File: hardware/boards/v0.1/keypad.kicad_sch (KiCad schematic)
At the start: 78 parts, among them SW1 TRIG1, SW10 TRIG10, SW11 TRIG11, SW12 TRIG12, SW13 TRIG13, SW14 TRIG14, SW15 TRIG15, SW16 TRIG16, SW17 MENU0, SW19 MENU1, SW2 TRIG2, SW20 MENU2, SW21 MENU3, SW3 TRIG3, SW4 TRIG4, SW5 TRIG5, SW6 TRIG6, SW7 TRIG7, SW8 TRIG8, SW9 TRIG9, U25 TCA8418RTWR, U38 ADS7128IRTER

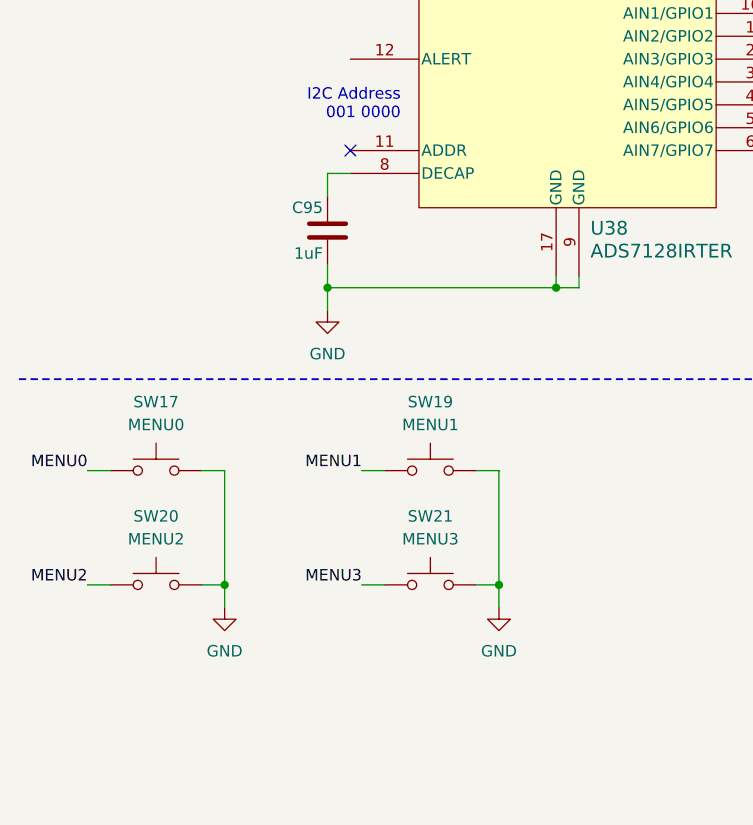
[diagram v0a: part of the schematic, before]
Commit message: feat: more routing and DRC cleanup
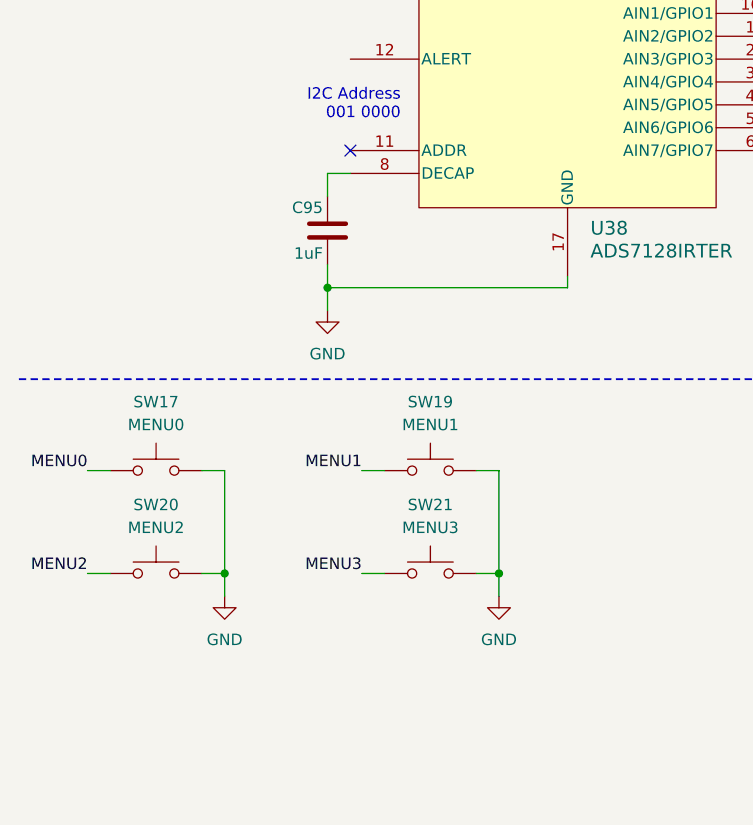
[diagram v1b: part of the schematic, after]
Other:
- moved on the sheet: SW20, SW21
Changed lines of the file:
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@@
 	)
 	(junction
-		(at 72.39 156.21)
-		(diameter 0)
-		(color 0 0 0 0)
-	)
-	(junction
-		(at 35.56 189.23)
+		(at 35.56 187.96)
 		(diameter 0)
 		(color 0 0 0 0)
@@
 	)
 	(junction
-		(at 66.04 189.23)
+		(at 66.04 187.96)
 		(diameter 0)
 		(color 0 0 0 0)
@@
 	(wire
 		(pts
-			(xy 46.99 156.21) (xy 72.39 156.21)
-		)
-		(stroke
-			(width 0)
-			(type default)
-		)
-	)
-	(wire
-		(pts
 			(xy 20.32 176.53) (xy 22.86 176.53)
 		)
@@
 	(wire
 		(pts
-			(xy 66.04 176.53) (xy 66.04 189.23)
+			(xy 66.04 176.53) (xy 66.04 187.96)
 		)
 		(stroke
@@
 	(wire
 		(pts
-			(xy 20.32 189.23) (xy 22.86 189.23)
+			(xy 20.32 187.96) (xy 22.86 187.96)
 		)
 		(stroke
@@
 	(wire
 		(pts
-			(xy 63.5 189.23) (xy 66.04 189.23)
+			(xy 63.5 187.96) (xy 66.04 187.96)
 		)
 		(stroke
@@
 	(wire
 		(pts
-			(xy 72.39 154.94) (xy 72.39 156.21)
-		)
-		(stroke
-			(width 0)
-			(type default)
-		)
-	)
-	(wire
-		(pts
 			(xy 198.12 81.28) (xy 200.66 81.28)
 		)
@@
 	(wire
 		(pts
-			(xy 35.56 176.53) (xy 35.56 189.23)
+			(xy 35.56 176.53) (xy 35.56 187.96)
 		)
 		(stroke
@@
 	(wire
 		(pts
-			(xy 33.02 189.23) (xy 35.56 189.23)
+			(xy 33.02 187.96) (xy 35.56 187.96)
 		)
 		(stroke
@@
 	(wire
 		(pts
-			(xy 50.8 189.23) (xy 53.34 189.23)
+			(xy 50.8 187.96) (xy 53.34 187.96)
 		)
 		(stroke
@@
 	(wire
 		(pts
-			(xy 72.39 156.21) (xy 74.93 156.21)
+			(xy 46.99 156.21) (xy 73.66 156.21)
 		)
 		(stroke
@@
 	(wire
 		(pts
-			(xy 35.56 189.23) (xy 35.56 191.77)
+			(xy 35.56 187.96) (xy 35.56 190.5)
 		)
 		(stroke
@@
 	(wire
 		(pts
-			(xy 66.04 189.23) (xy 66.04 191.77)
+			(xy 66.04 187.96) (xy 66.04 190.5)
 		)
 		(stroke
@@
 	(wire
 		(pts
-			(xy 74.93 154.94) (xy 74.93 156.21)
+			(xy 162.56 142.24) (xy 163.83 142.24)
 		)
 		(stroke
@@
 	(wire
 		(pts
-			(xy 162.56 142.24) (xy 163.83 142.24)
+			(xy 137.16 35.56) (xy 135.89 35.56)
 		)
 		(stroke
@@
 	(wire
 		(pts
-			(xy 137.16 35.56) (xy 135.89 35.56)
+			(xy 162.56 66.04) (xy 161.29 66.04)
 		)
 		(stroke
@@
 	(wire
 		(pts
-			(xy 162.56 66.04) (xy 161.29 66.04)
+			(xy 134.62 134.62) (xy 138.43 134.62)
 		)
 		(stroke
@@
 	(wire
 		(pts
-			(xy 134.62 134.62) (xy 138.43 134.62)
+			(xy 73.66 154.94) (xy 73.66 156.21)
 		)
 		(stroke
@@
 	)
 	(label "MENU2"
-		(at 20.32 189.23 180)
+		(at 20.32 187.96 180)
 		(effects
 			(font
@@
 	)
 	(label "MENU3"
-		(at 50.8 189.23 180)
+		(at 50.8 187.96 180)
 		(effects
 			(font
@@
 	(symbol
 		(lib_id "Switch:SW_Push")
-		(at 58.42 189.23 0)
+		(at 58.42 187.96 0)
 		(unit 1)
 		(exclude_from_sim no)
@@
 		(fields_autoplaced yes)
 		(property "Reference" "SW21"
-			(at 58.42 181.61 0)
+			(at 58.42 180.34 0)
 			(effects
 				(font
@@
 		)
 		(property "Value" "MENU3"
-			(at 58.42 184.15 0)
+			(at 58.42 182.88 0)
 			(effects
 				(font
@@
 		)
 		(property "Footprint" "Button_Switch_SMD:SW_SPST_B3S-1000"
-			(at 58.42 184.15 0)
+			(at 58.42 182.88 0)
 			(effects
 				(font
@@
 		)
 		(property "Datasheet" "~"
-			(at 58.42 184.15 0)
+			(at 58.42 182.88 0)
 			(effects
 				(font
@@
 		)
 		(property "Description" "Push button switch, generic, two pins"
-			(at 58.42 189.23 0)
+			(at 58.42 187.96 0)
 			(effects
 				(font
@@
 		)
 		(property "MANUFACTURER" ""
-			(at 58.42 189.23 0)
+			(at 58.42 187.96 0)
 			(effects
 				(font
@@
 		)
 		(property "MAXIMUM_PACKAGE_HEIGHT" ""
-			(at 58.42 189.23 0)
+			(at 58.42 187.96 0)
 			(effects
 				(font
@@
 		)
 		(property "PARTREV" ""
-			(at 58.42 189.23 0)
+			(at 58.42 187.96 0)
 			(effects
 				(font
@@
 		)
 		(property "STANDARD" ""
-			(at 58.42 189.23 0)
+			(at 58.42 187.96 0)
 			(effects
 				(font
@@
 		)
 		(property "Connector" ""
-			(at 58.42 189.23 0)
+			(at 58.42 187.96 0)
 			(effects
 				(font
@@
 	(symbol
 		(lib_id "power:GND")
-		(at 66.04 191.77 0)
+		(at 66.04 190.5 0)
 		(unit 1)
 		(exclude_from_sim no)
@@
 		(dnp no)
 		(property "Reference" "#PWR042"
-			(at 66.04 198.12 0)
+			(at 66.04 196.85 0)
 			(effects
 				(font
@@
 		)
 		(property "Value" "GND"
-			(at 66.04 196.596 0)
+			(at 66.04 195.326 0)
 			(effects
 				(font
@@
 		)
 		(property "Footprint" ""
-			(at 66.04 191.77 0)
+			(at 66.04 190.5 0)
 			(effects
 				(font
@@
 		)
 		(property "Datasheet" ""
-			(at 66.04 191.77 0)
+			(at 66.04 190.5 0)
 			(effects
 				(font
@@
 		)
 		(property "Description" "Power symbol creates a global label with name \"GND\" , ground"
-			(at 66.04 191.77 0)
+			(at 66.04 190.5 0)
 			(effects
 				(font
@@
 	(symbol
 		(lib_id "Switch:SW_Push")
-		(at 27.94 189.23 0)
+		(at 27.94 187.96 0)
 		(unit 1)
 		(exclude_from_sim no)
@@
 		(fields_autoplaced yes)
 		(property "Reference" "SW20"
-			(at 27.94 181.61 0)
+			(at 27.94 180.34 0)
 			(effects
 				(font
@@
 		)
 		(property "Value" "MENU2"
-			(at 27.94 184.15 0)
+			(at 27.94 182.88 0)
 			(effects
 				(font
@@
 		)
 		(property "Footprint" "Button_Switch_SMD:SW_SPST_B3S-1000"
-			(at 27.94 184.15 0)
+			(at 27.94 182.88 0)
 			(effects
 				(font
@@
 		)
 		(property "Datasheet" "~"
-			(at 27.94 184.15 0)
+			(at 27.94 182.88 0)
 			(effects
 				(font
@@
 		)
 		(property "Description" "Push button switch, generic, two pins"
-			(at 27.94 189.23 0)
+			(at 27.94 187.96 0)
 			(effects
 				(font
@@
 		)
 		(property "MANUFACTURER" ""
-			(at 27.94 189.23 0)
+			(at 27.94 187.96 0)
 			(effects
 				(font
@@
 		)
 		(property "MAXIMUM_PACKAGE_HEIGHT" ""
-			(at 27.94 189.23 0)
+			(at 27.94 187.96 0)
 			(effects
 				(font
@@
 		)
 		(property "PARTREV" ""
-			(at 27.94 189.23 0)
+			(at 27.94 187.96 0)
 			(effects
 				(font
@@
 		)
 		(property "STANDARD" ""
-			(at 27.94 189.23 0)
+			(at 27.94 187.96 0)
 			(effects
 				(font
@@
 		)
 		(property "Connector" ""
-			(at 27.94 189.23 0)
+			(at 27.94 187.96 0)
 			(effects
 				(font
@@
 	(symbol
 		(lib_id "power:GND")
-		(at 35.56 191.77 0)
+		(at 35.56 190.5 0)
 		(unit 1)
 		(exclude_from_sim no)
@@
 		(dnp no)
 		(property "Reference" "#PWR036"
-			(at 35.56 198.12 0)
+			(at 35.56 196.85 0)
 			(effects
 				(font
@@
 		)
 		(property "Value" "GND"
-			(at 35.56 196.596 0)
+			(at 35.56 195.326 0)
 			(effects
 				(font
@@
 		)
 		(property "Footprint" ""
-			(at 35.56 191.77 0)
+			(at 35.56 190.5 0)
 			(effects
 				(font
@@
 		)
 		(property "Datasheet" ""
-			(at 35.56 191.77 0)
+			(at 35.56 190.5 0)
 			(effects
 				(font
@@
 		)
 		(property "Description" "Power symbol creates a global label with name \"GND\" , ground"
-			(at 35.56 191.77 0)
+			(at 35.56 190.5 0)
 			(effects
 				(font

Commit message: feat: more DRC cleanup
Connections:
- net VELOCITY_ALERT: now reaches U38.12 (ALERT)
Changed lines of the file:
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@@
+	(wire
+		(pts
+			(xy 46.99 130.81) (xy 49.53 130.81)
+		)
+		(stroke
+			(width 0)
+			(type default)
+		)
+	)
 	(wire
 		(pts
@@
 		)
 	)
+	(hierarchical_label "VELOCITY_ALERT"
+		(shape output)
+		(at 46.99 130.81 180)
+		(effects
+			(font
+				(size 1.27 1.27)
+			)
+			(justify right)
+		)
+	)

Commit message: feat: routing cleanup and start of BOM selection
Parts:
- C93, C94, C95: JLC (none) -> C14445
- R18: JLC (none) -> C25531
- SW1, SW10, SW11, SW12, SW13, SW14, SW15, SW16, SW17, SW19, SW2, SW20, SW21, SW3, SW4, SW5, SW6, SW7, SW8, SW9, TP1, TP10, TP11, TP12, TP13, TP16, TP17, TP18, TP2, TP3, TP4, TP5, TP6, TP7, TP8, TP9: now left out of the parts list
- U38: JLC (none) -> C2867992
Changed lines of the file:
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@@
 		(unit 1)
 		(exclude_from_sim no)
-		(in_bom yes)
+		(in_bom no)
 		(on_board yes)
 		(dnp no)
@@
 		(unit 1)
 		(exclude_from_sim no)
-		(in_bom yes)
+		(in_bom no)
 		(on_board yes)
 		(dnp no)
@@
 		(unit 1)
 		(exclude_from_sim no)
-		(in_bom yes)
+		(in_bom no)
 		(on_board yes)
 		(dnp no)
@@
 		(unit 1)
 		(exclude_from_sim no)
-		(in_bom yes)
+		(in_bom no)
 		(on_board yes)
 		(dnp no)
@@
 		(unit 2)
 		(exclude_from_sim no)
-		(in_bom yes)
+		(in_bom no)
 		(on_board yes)
 		(dnp no)
@@
 		(unit 1)
 		(exclude_from_sim no)
-		(in_bom yes)
+		(in_bom no)
 		(on_board yes)
 		(dnp no)
@@
 		(unit 2)
 		(exclude_from_sim no)
-		(in_bom yes)
+		(in_bom no)
 		(on_board yes)
 		(dnp no)
@@
 		(unit 1)
 		(exclude_from_sim no)
-		(in_bom yes)
+		(in_bom no)
 		(on_board yes)
 		(dnp no)
@@
 		(unit 2)
 		(exclude_from_sim no)
-		(in_bom yes)
+		(in_bom no)
 		(on_board yes)
 		(dnp no)
@@
 		(unit 2)
 		(exclude_from_sim no)
-		(in_bom yes)
+		(in_bom no)
 		(on_board yes)
 		(dnp no)
@@
 		(unit 1)
 		(exclude_from_sim no)
-		(in_bom yes)
+		(in_bom no)
 		(on_board yes)
 		(dnp no)
@@
 		(unit 1)
 		(exclude_from_sim no)
-		(in_bom yes)
+		(in_bom no)
 		(on_board yes)
 		(dnp no)
@@
 		(unit 1)
 		(exclude_from_sim no)
-		(in_bom yes)
+		(in_bom no)
 		(on_board yes)
 		(dnp no)
@@
 		(unit 2)
 		(exclude_from_sim no)
-		(in_bom yes)
+		(in_bom no)
 		(on_board yes)
 		(dnp no)
@@
 		(unit 2)
 		(exclude_from_sim no)
-		(in_bom yes)
+		(in_bom no)
 		(on_board yes)
 		(dnp no)
@@
 		(unit 1)
 		(exclude_from_sim no)
-		(in_bom yes)
+		(in_bom no)
 		(on_board yes)
 		(dnp no)
@@
 		(unit 1)
 		(exclude_from_sim no)
-		(in_bom yes)
+		(in_bom no)
 		(on_board yes)
 		(dnp no)
@@
 		(unit 1)
 		(exclude_from_sim no)
-		(in_bom yes)
+		(in_bom no)
 		(on_board yes)
 		(dnp no)
@@
 		(unit 2)
 		(exclude_from_sim no)
-		(in_bom yes)
+		(in_bom no)
 		(on_board yes)
 		(dnp no)
@@
 		(unit 1)
 		(exclude_from_sim no)
-		(in_bom yes)
+		(in_bom no)
 		(on_board yes)
 		(dnp no)
@@
 		(unit 1)
 		(exclude_from_sim no)
-		(in_bom yes)
+		(in_bom no)
 		(on_board yes)
 		(dnp no)
@@
 		(unit 1)
 		(exclude_from_sim no)
-		(in_bom yes)
+		(in_bom no)
 		(on_board yes)
 		(dnp no)
@@
 			)
 		)
+		(property "JLC" "C25531"
+			(at 57.15 29.21 0)
+			(effects
+				(font
+					(size 1.27 1.27)
+				)
+				(hide yes)
+			)
+		)
 		(pin "2"
 		)
@@
 		(unit 1)
 		(exclude_from_sim no)
-		(in_bom yes)
+		(in_bom no)
 		(on_board yes)
 		(dnp no)
@@
 			)
 		)
+		(property "JLC" "C2867992"
+			(at 73.66 132.08 0)
+			(effects
+				(font
+					(size 1.27 1.27)
+				)
+				(hide yes)
+			)
+		)
 		(pin "7"
 		)
@@
 		(unit 1)
 		(exclude_from_sim no)
-		(in_bom yes)
+		(in_bom no)
 		(on_board yes)
 		(dnp no)
@@
 		(unit 1)
 		(exclude_from_sim no)
-		(in_bom yes)
+		(in_bom no)
 		(on_board yes)
 		(dnp no)
@@
 		(unit 1)
 		(exclude_from_sim no)
-		(in_bom yes)
+		(in_bom no)
 		(on_board yes)
 		(dnp no)
@@
 		(unit 1)
 		(exclude_from_sim no)
-		(in_bom yes)
+		(in_bom no)
 		(on_board yes)
 		(dnp no)
@@
 		(unit 1)
 		(exclude_from_sim no)
-		(in_bom yes)
+		(in_bom no)
 		(on_board yes)
 		(dnp no)
@@
 		(unit 1)
 		(exclude_from_sim no)
-		(in_bom yes)
+		(in_bom no)
 		(on_board yes)
 		(dnp no)
@@
 		(unit 2)
 		(exclude_from_sim no)
-		(in_bom yes)
+		(in_bom no)
 		(on_board yes)
 		(dnp no)
@@
 		(unit 1)
 		(exclude_from_sim no)
-		(in_bom yes)
+		(in_bom no)
 		(on_board yes)
 		(dnp no)
@@
 		(unit 1)
 		(exclude_from_sim no)
-		(in_bom yes)
+		(in_bom no)
 		(on_board yes)
 		(dnp no)
@@
 		(unit 1)
 		(exclude_from_sim no)
-		(in_bom yes)
+		(in_bom no)
 		(on_board yes)
 		(dnp no)
@@
 		(unit 2)
 		(exclude_from_sim no)
-		(in_bom yes)
+		(in_bom no)
 		(on_board yes)
 		(dnp no)
@@
 		(unit 1)
 		(exclude_from_sim no)
-		(in_bom yes)
+		(in_bom no)
 		(on_board yes)
 		(dnp no)
@@
 		(unit 1)
 		(exclude_from_sim no)
-		(in_bom yes)
+		(in_bom no)
 		(on_board yes)
 		(dnp no)
@@
 		(unit 2)
 		(exclude_from_sim no)
-		(in_bom yes)
+		(in_bom no)
 		(on_board yes)
 		(dnp no)
@@
 			)
 		)
+		(property "JLC" "C14445"
+			(at 67.31 105.41 0)
+			(effects
+				(font
+					(size 1.27 1.27)
+				)
+				(hide yes)
+			)
+		)
 		(pin "2"
 		)
@@
 		(unit 1)
 		(exclude_from_sim no)
-		(in_bom yes)
+		(in_bom no)
 		(on_board yes)
 		(dnp no)
@@
 		(unit 1)
 		(exclude_from_sim no)
-		(in_bom yes)
+		(in_bom no)
 		(on_board yes)
 		(dnp no)
@@
 		(unit 2)
 		(exclude_from_sim no)
-		(in_bom yes)
+		(in_bom no)
 		(on_board yes)
 		(dnp no)
@@
 		(unit 2)
 		(exclude_from_sim no)
-		(in_bom yes)
+		(in_bom no)
 		(on_board yes)
 		(dnp no)
@@
 			)
 		)
+		(property "JLC" "C14445"
+			(at 80.01 105.41 0)
+			(effects
+				(font
+					(size 1.27 1.27)
+				)
+				(hide yes)
+			)
+		)
 		(pin "2"
 		)
@@
 			)
 		)
+		(property "JLC" "C14445"
+			(at 46.99 149.86 0)
+			(effects
+				(font
+					(size 1.27 1.27)
+				)
+				(hide yes)
+			)
+		)
 		(pin "2"
 		)
@@
 		(unit 2)
 		(exclude_from_sim no)
-		(in_bom yes)
+		(in_bom no)
 		(on_board yes)
 		(dnp no)
@@
 		(unit 1)
 		(exclude_from_sim no)
-		(in_bom yes)
+		(in_bom no)
 		(on_board yes)
 		(dnp no)
@@
 		(unit 1)
 		(exclude_from_sim no)
-		(in_bom yes)
+		(in_bom no)
 		(on_board yes)
 		(dnp no)
@@
 		(unit 1)
 		(exclude_from_sim no)
-		(in_bom yes)
+		(in_bom no)
 		(on_board yes)
 		(dnp no)
@@
 		(unit 2)
 		(exclude_from_sim no)
-		(in_bom yes)
+		(in_bom no)
 		(on_board yes)
 		(dnp no)
@@
 		(unit 2)
 		(exclude_from_sim no)
-		(in_bom yes)
+		(in_bom no)
 		(on_board yes)
 		(dnp no)
@@
 		(unit 2)
 		(exclude_from_sim no)
-		(in_bom yes)
+		(in_bom no)
 		(on_board yes)
 		(dnp no)
@@
 		(unit 1)
 		(exclude_from_sim no)
-		(in_bom yes)
+		(in_bom no)
 		(on_board yes)
 		(dnp no)
@@
 		(unit 1)
 		(exclude_from_sim no)
-		(in_bom yes)
+		(in_bom no)
 		(on_board yes)
 		(dnp no)
@@
 		(unit 1)
 		(exclude_from_sim no)
-		(in_bom yes)
+		(in_bom no)
 		(on_board yes)
 		(dnp no)
@@
 		(unit 1)
 		(exclude_from_sim no)
-		(in_bom yes)
+		(in_bom no)
 		(on_board yes)
 		(dnp no)

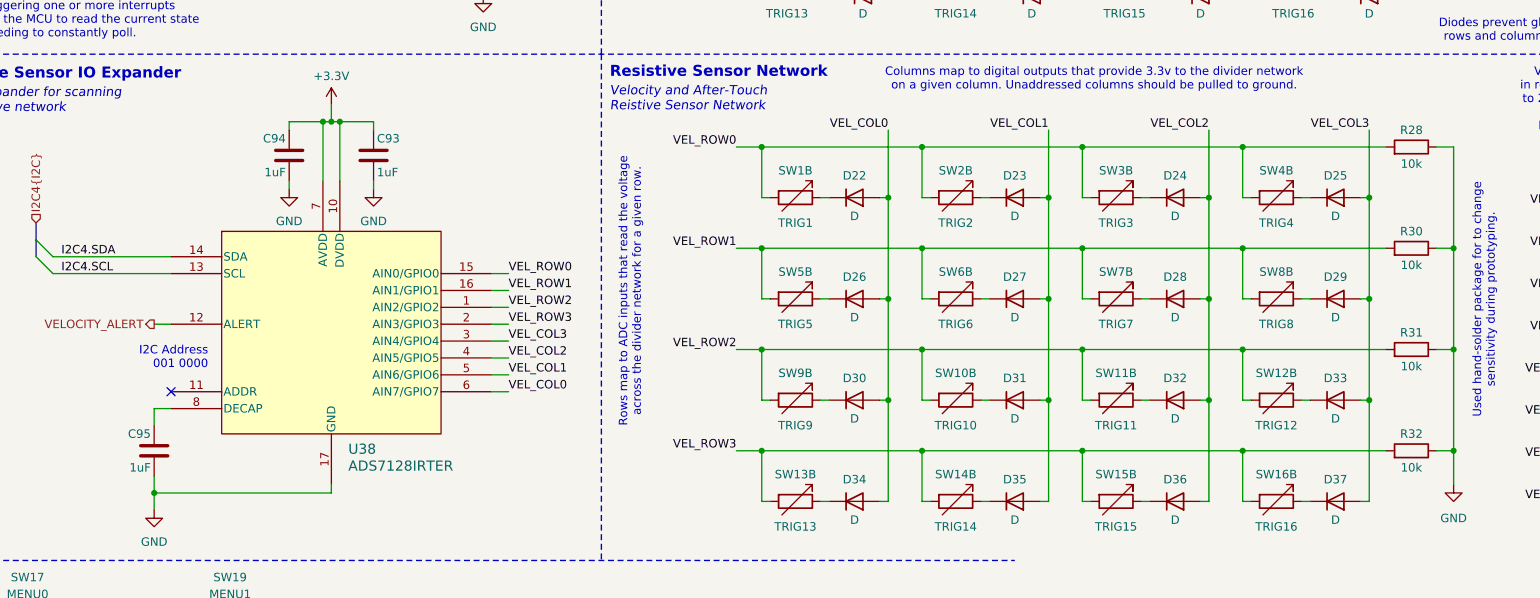
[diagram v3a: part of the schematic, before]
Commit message: feat: update various components to 0402
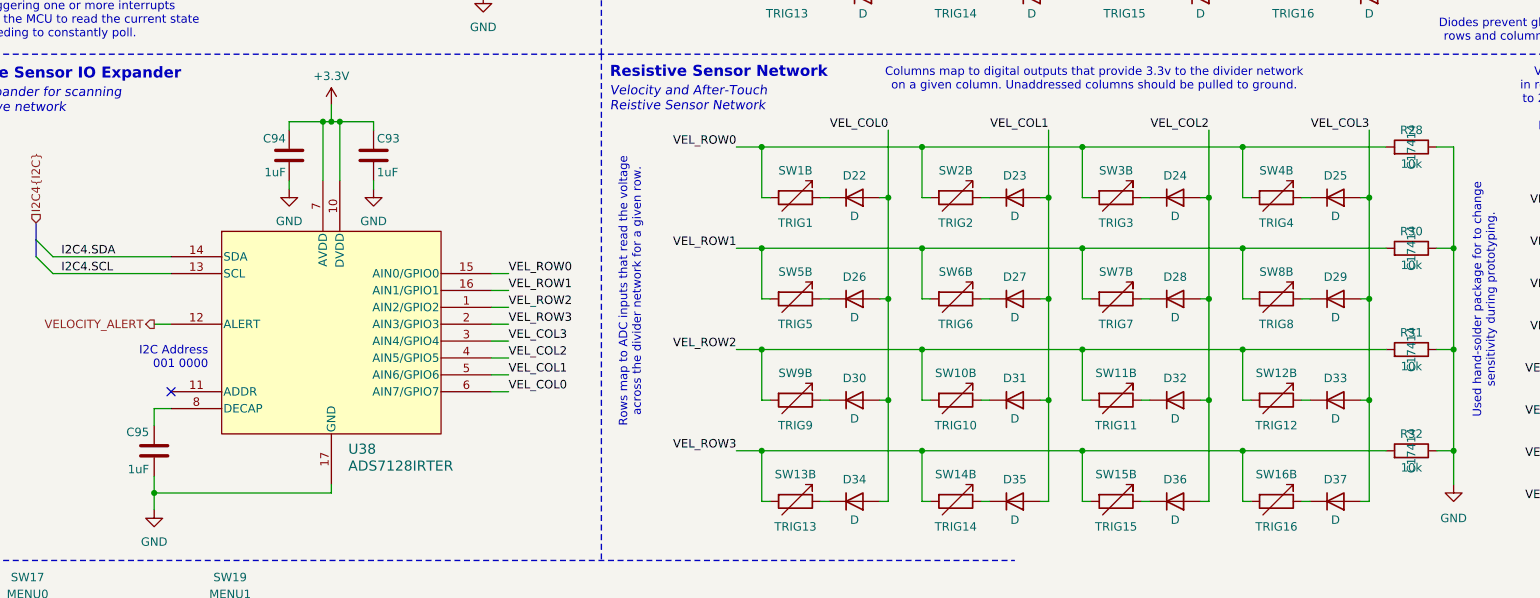
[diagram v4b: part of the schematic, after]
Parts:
- R28, R30, R31, R32: JLC (none) -> C17414
